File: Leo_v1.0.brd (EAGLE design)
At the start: 68.6 x 53.3 mm, 60 parts, among them CN1 POWER_JACK, CN2 47346-0001, CN3 DIGITAL10, CN4 DIGITAL8, CN5 ICSP, CN6 POWER8, CN7 ANALOG6, IC1 AMS1117-5.0, IC2 AMS1117-3.3, IC3 MCP6002T-I/SN, Q1 12MHz, Q2 16MHz, T1 AO3401A, T2 2N7002, U1 CH340G

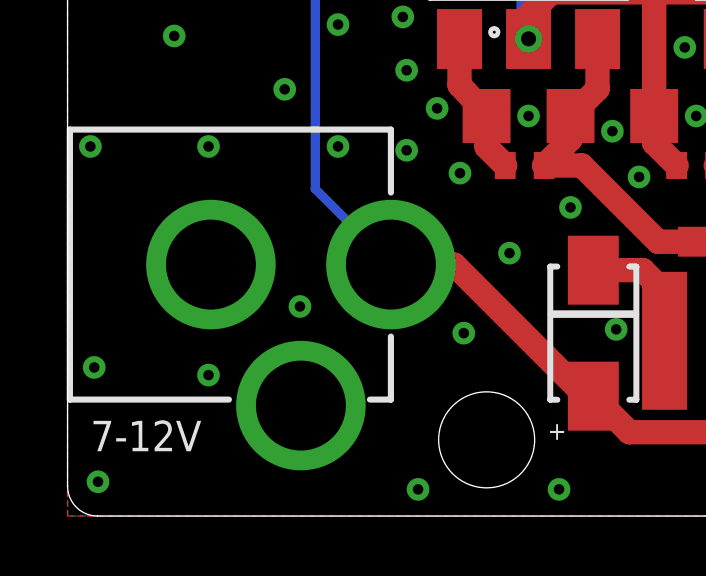
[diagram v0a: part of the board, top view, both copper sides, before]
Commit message: Add extra traces around power jack.
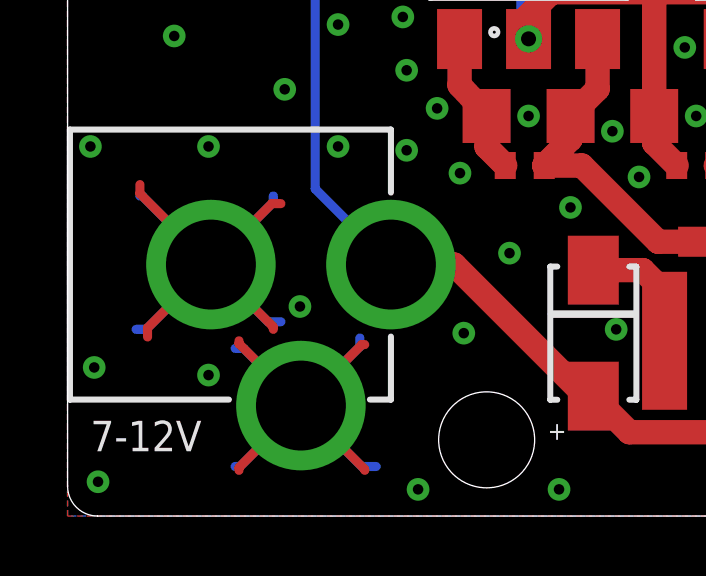
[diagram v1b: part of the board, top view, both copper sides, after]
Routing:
- net GND: track 52.0 -> 102.5 mm

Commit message: Add some routing for Leo.
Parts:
- removed C10: 12pF, rcl:C0402
- removed C18, C8: 100nF, rcl:C0402
- removed Q1: 12MHz, crystal-geyer_V1_0:3.2X2.5_KX-7
- removed R11: 1K, rcl:R0402
- removed SJ1: USB_RESET, _my_jumpers:SJ
- added L3: GZ2012D601TF, Wurth_Automotive_WE-CBA:WE-CBA_0805(W=4)
- added U2: ATMEGA32U4-AU, SparkFun-IC-Microcontroller:TQFP44
- C7: value 100nF -> 1uF; device rcl:C0402 -> rcl:C0603
- C9: value 12pF -> 100nF
- R3: value 1M -> 10K
- U1: value CH340G -> ATMEGA32U4-MU; device SparkFun-IC-Comms:SO016 -> SparkFun-IC-Microcontroller:QFN-44
- moved C7 43.2 mm to (59.7, 30.7)
- moved C9 36.5 mm to (54.9, 23.4), turned to 180 degrees
- moved U1 35.0 mm to (51.1, 30.7), turned to 180 degrees
- moved R3 27.1 mm to (43.8, 26.0), turned to 90 degrees
- moved R12 25.6 mm to (55.1, 38.2), turned to 0 degrees
- moved C14 13.9 mm to (59.8, 27.3)
- moved C12 7.12 mm to (51.9, 40.9)
- moved C13 7.12 mm to (49.1, 40.9)
- moved Q2 7.12 mm to (50.7, 43.1)
- moved R6 7.12 mm to (51.1, 39.5)
- moved C17 6.08 mm to (55.1, 41.0), turned to 180 degrees
- moved C15 6.03 mm to (54.0, 39.4), turned to 180 degrees
- moved C19 5.72 mm to (53.6, 22.0)
- moved C16 1.15 mm to (46.7, 22.9)
- moved R4 0.64 mm to (9.91, 31.1)
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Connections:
- removed net A4_SDA: CN3.2, CN7.2
- removed net A5_SCL: CN3.1, CN7.1
- removed net D2: CN4.6
- removed net D3_PWM: CN4.5
- removed net N$5: C18.2, SJ1.1
- removed net N$6: C7.2, U1.4
- removed net USB_DTR: C18.1, R11.2, U1.13
- removed net USB_OSC_IN: C9.2, Q1.3, R3.2, U1.7
- removed net USB_OSC_OUT: C10.2, Q1.1, R3.1, U1.8
- new net A4: CN7.2, U1.40, U2.40
- new net A5: CN7.1, U1.41, U2.41
- new net AVCC: C9.1, L3.1, U1.24, U1.44, U2.24, U2.44
- new net D2_SDA: CN3.2, CN4.6, U1.19, U2.19
- new net D3_SCL: CN3.1, CN4.5, U1.18, U2.18
- new net HWB: R3.2, U1.33, U2.33
- new net RX_LED: R8.1, U1.8, U2.8
- new net SPI_MISO: CN5.1, U1.11, U2.11
- new net SPI_MOSI: CN5.4, U1.10, U2.10
- new net SPI_SCK: CN5.3, U1.9, U2.9
- new net TX_LED: R9.1, U1.22, U2.22
- new net UCAP: C7.1, U1.6, U2.6
- net 5V: now also L3.2, U1.14, U1.2, U1.34, U2.14, U2.2, U2.34; no longer C8.1, U1.16
- net A0: now also U1.36, U2.36
- net A1: now also U1.37, U2.37
- net A2: now also U1.38, U2.38
- net A3: now also U1.39, U2.39
- net AREF: now also U1.42, U2.42
- net D0_RX: now also U1.20, U2.20; no longer R8.1, U1.2
- net D10_SS: now also U1.30, U2.30
- net D11_MOSI: now also U1.12, U2.12; no longer CN5.4
- net D12_MISO: now also U1.26, U2.26; no longer CN5.1
- net D13_SCK: now also U1.32, U2.32; no longer CN5.3
- net D1_TX: now also U1.21, U2.21; no longer R9.1, U1.3
- net D4: now also U1.25, U2.25
- net D5_PWM: now also U1.31, U2.31
- net D6_PWM: now also U1.27, U2.27
- net D7: now also U1.1, U2.1
- net D8: now also U1.28, U2.28
- net D9_PWM: now also U1.29, U2.29
- net GND: now also C7.2, C9.2, R3.1, U1.15, U1.23, U1.35, U1.43, U1.5, U2.15, U2.23, U2.35, U2.43, U2.5; no longer C10.1, C7.1, C8.2, C9.1, R11.1, U1.1
- net MCU_OSC_IN: now also U1.16, U2.16
- net MCU_OSC_OUT: now also U1.17, U2.17
- net RESET: now also U1.13, U2.13; no longer SJ1.2
- net USB_D_M: now also U1.3, U2.3; no longer U1.6
- net USB_D_P: now also U1.4, U2.4; no longer U1.5
- net VUSB: now also U1.7, U2.7
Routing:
- net A5_SCL: track 92.3 -> 0.00 mm, vias 2 -> 0
- net A4_SDA: track 89.7 -> 0.00 mm, vias 2 -> 0
- net RX_LED: track 0.00 -> 81.7 mm, vias 0 -> 4
- net VUSB: track 18.9 -> 83.8 mm, vias 2 -> 4
- net D1_TX: track 91.9 -> 31.4 mm, vias 4 -> 2
- net TX_LED: track 0.00 -> 57.8 mm, vias 0 -> 2
- net D2_SDA: track 0.00 -> 56.8 mm, vias 0 -> 3
- net D0_RX: track 87.7 -> 32.8 mm, vias 4 -> 2
- net D3_SCL: track 0.00 -> 54.5 mm, vias 0 -> 2
- net USB_D_P: track 8.97 -> 56.2 mm, vias 0 -> 2
- net USB_D_M: track 8.91 -> 56.1 mm, vias 0 -> 2
- net D12_MISO: track 69.0 -> 30.9 mm, vias 3 -> 1
- net A5: track 0.00 -> 29.5 mm, vias 0 -> 1
- net AVCC: track 0.00 -> 28.8 mm, vias 0 -> 2
- net A4: track 0.00 -> 28.7 mm, vias 0 -> 1
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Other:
- board text added: "LEO"
- board text removed: "UNO"

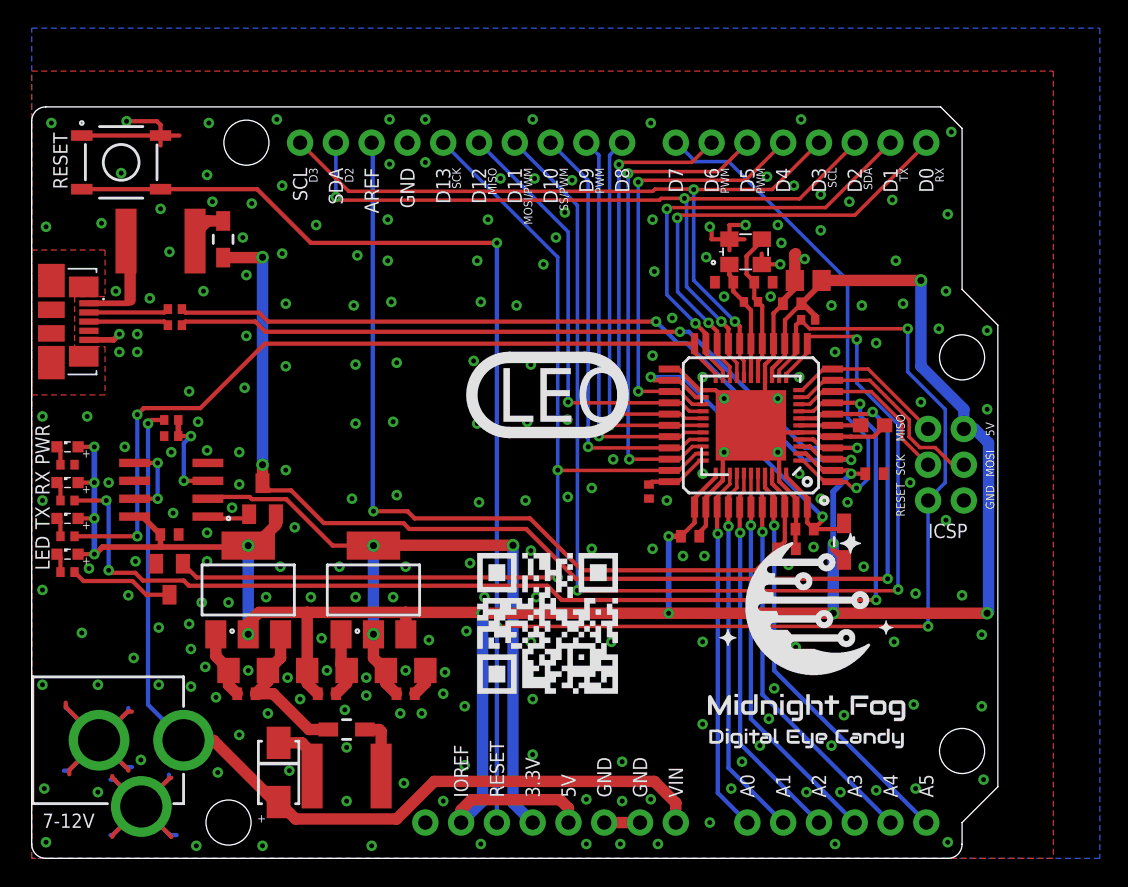
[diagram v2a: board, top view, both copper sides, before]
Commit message: Moved some traces around
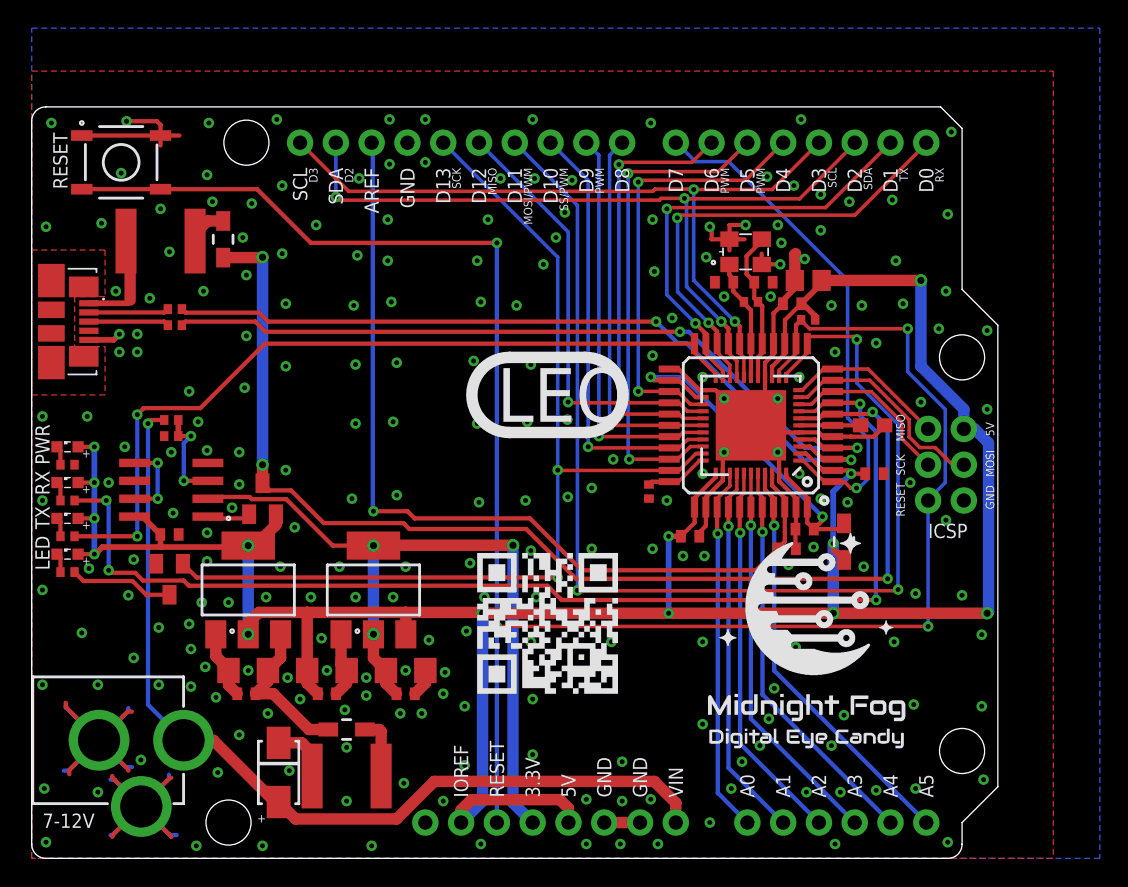
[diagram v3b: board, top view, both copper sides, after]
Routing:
- net GND: vias 231 -> 232

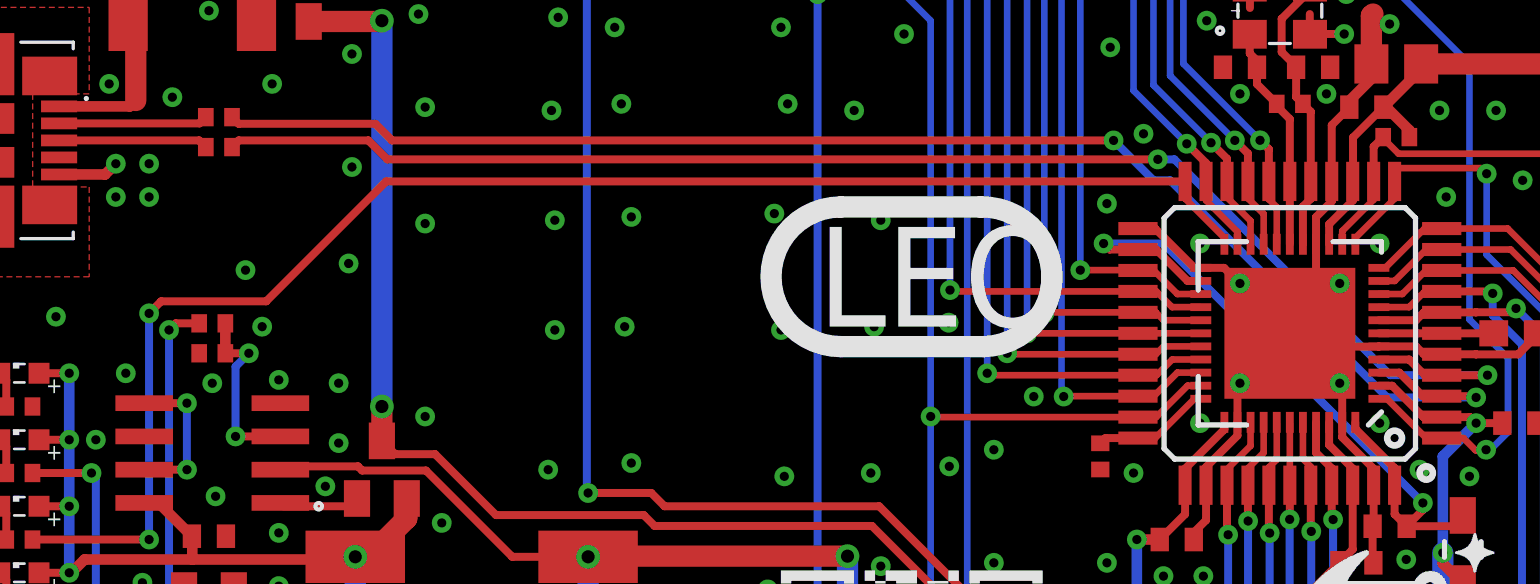
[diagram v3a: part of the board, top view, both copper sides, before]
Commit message: Moved TX_LED line away from USB lines to prevent interference.
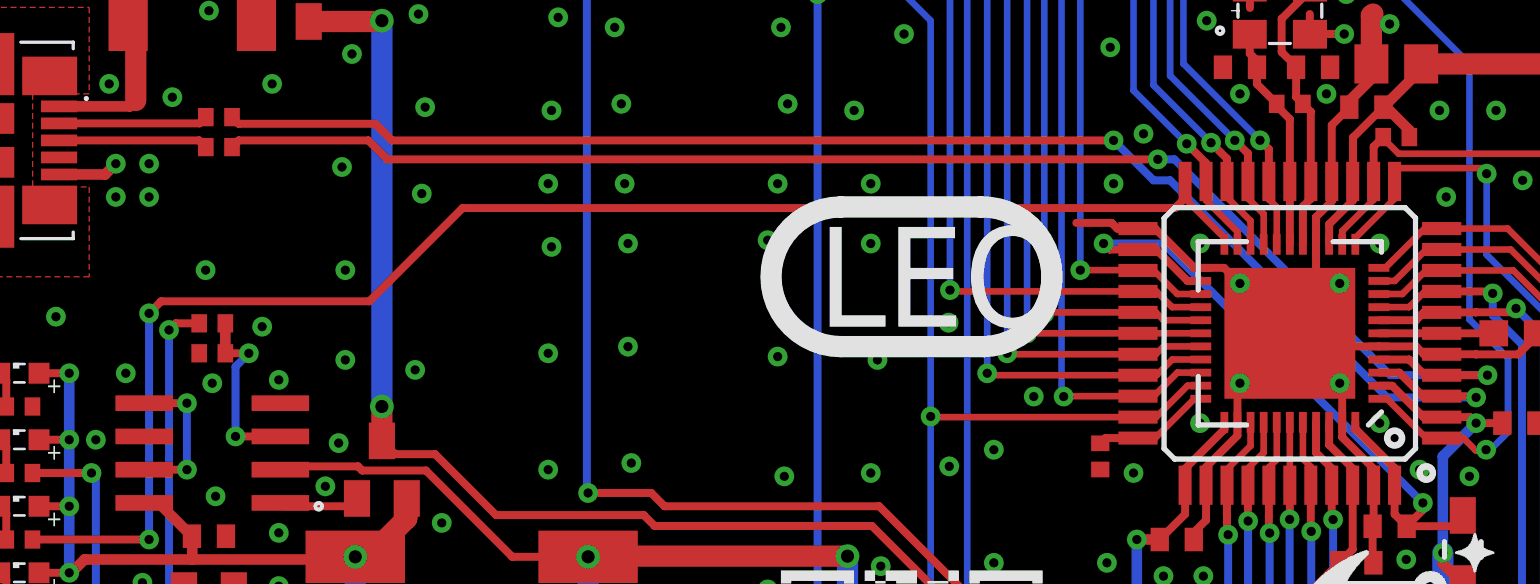
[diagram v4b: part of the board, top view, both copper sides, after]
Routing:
- net GND: track 124.3 -> 127.0 mm, vias 232 -> 236
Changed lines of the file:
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@@
 <via x="50.673" y="44.958" extent="1-16" drill="0.35"/>
 <via x="49.149" y="39.878" extent="1-16" drill="0.35"/>
-<via x="18.034" y="34.925" extent="1-16" drill="0.35"/>
+<via x="17.907" y="36.068" extent="1-16" drill="0.35"/>
 <via x="22.733" y="25.527" extent="1-16" drill="0.35"/>
 <via x="18.669" y="23.495" extent="1-16" drill="0.35"/>
@@
 <via x="9.144" y="46.101" extent="1-16" drill="0.35"/>
 <via x="14.732" y="26.543" extent="1-16" drill="0.35"/>
-<via x="22.987" y="30.861" extent="1-16" drill="0.35"/>
-<via x="14.732" y="28.829" extent="1-16" drill="0.35"/>
+<via x="22.86" y="34.036" extent="1-16" drill="0.35"/>
+<via x="14.986" y="29.718" extent="1-16" drill="0.35"/>
 <via x="12.446" y="23.114" extent="1-16" drill="0.35"/>
 <via x="9.906" y="28.829" extent="1-16" drill="0.35"/>
@@
 <via x="67.564" y="5.588" extent="1-16" drill="0.35"/>
 <via x="65.024" y="1.143" extent="1-16" drill="0.35"/>
-<via x="15.24" y="37.084" extent="1-16" drill="0.35"/>
+<via x="14.859" y="37.084" extent="1-16" drill="0.35"/>
 <via x="14.986" y="44.069" extent="1-16" drill="0.35"/>
 <via x="15.621" y="46.482" extent="1-16" drill="0.35"/>
@@
 <wire x1="5.812" y1="36.8" x2="6.223" y2="37.211" width="0.4064" layer="1"/>
 <via x="35.052" y="25.4" extent="1-16" drill="0.35"/>
-<via x="31.623" y="30.861" extent="1-16" drill="0.35"/>
-<via x="35.179" y="30.988" extent="1-16" drill="0.35"/>
+<via x="31.115" y="34.29" extent="1-16" drill="0.35"/>
+<via x="35.052" y="34.163" extent="1-16" drill="0.35"/>
 <via x="41.91" y="4.064" extent="1-16" drill="0.35"/>
 <via x="44.45" y="1.016" extent="1-16" drill="0.35"/>
@@
 <via x="15.24" y="41.402" extent="1-16" drill="0.35"/>
 <via x="17.78" y="42.926" extent="1-16" drill="0.35"/>
-<via x="18.034" y="27.559" extent="1-16" drill="0.35"/>
-<via x="25.654" y="30.988" extent="1-16" drill="0.35"/>
+<via x="17.653" y="29.337" extent="1-16" drill="0.35"/>
+<via x="25.781" y="34.163" extent="1-16" drill="0.35"/>
 <via x="25.908" y="25.781" extent="1-16" drill="0.35"/>
-<via x="11.176" y="33.147" extent="1-16" drill="0.35"/>
-<via x="22.987" y="35.052" extent="1-16" drill="0.35"/>
+<via x="9.652" y="33.147" extent="1-16" drill="0.35"/>
+<via x="22.733" y="36.449" extent="1-16" drill="0.35"/>
 <via x="32.131" y="18.542" extent="1-16" drill="0.35"/>
 <via x="31.115" y="20.955" extent="1-16" drill="0.35"/>
@@
 <wire x1="52.054" y1="34.134" x2="52.054" y2="32.6658" width="0.3048" layer="1"/>
 <wire x1="52.054" y1="32.6658" x2="52.07" y2="32.6498" width="0.3048" layer="1"/>
-<wire x1="54.454" y1="30.234" x2="54.446" y2="30.226" width="0.3048" layer="1"/>
-<wire x1="54.446" y1="30.226" x2="52.9698" y2="30.226" width="0.3048" layer="1"/>
 <wire x1="53.054" y1="27.334" x2="53.054" y2="28.5962" width="0.3048" layer="1"/>
 <wire x1="53.054" y1="28.5962" x2="52.959" y2="28.6912" width="0.3048" layer="1"/>
@@
 <via x="44.069" y="45.339" extent="1-16" drill="0.35"/>
 <via x="44.196" y="41.656" extent="1-16" drill="0.35"/>
-<via x="44.069" y="35.687" extent="1-16" drill="0.35"/>
+<via x="44.323" y="36.449" extent="1-16" drill="0.35"/>
 <via x="56.007" y="25.527" extent="1-16" drill="0.35"/>
 <via x="57.912" y="25.273" extent="1-16" drill="0.35"/>
@@
 <via x="31.877" y="39.497" extent="1-16" drill="0.35"/>
 <via x="25.527" y="39.497" extent="1-16" drill="0.35"/>
-<via x="31.369" y="35.306" extent="1-16" drill="0.35"/>
-<via x="25.908" y="35.179" extent="1-16" drill="0.35"/>
+<via x="31.496" y="36.449" extent="1-16" drill="0.35"/>
+<via x="25.654" y="36.449" extent="1-16" drill="0.35"/>
 <via x="22.86" y="39.243" extent="1-16" drill="0.35"/>
 <via x="23.114" y="42.799" extent="1-16" drill="0.35"/>
@@
 <via x="17.78" y="47.752" extent="1-16" drill="0.35"/>
 <via x="18.034" y="39.37" extent="1-16" drill="0.35"/>
-<via x="15.113" y="33.401" extent="1-16" drill="0.35"/>
+<via x="14.986" y="33.147" extent="1-16" drill="0.35"/>
 <via x="11.811" y="30.988" extent="1-16" drill="0.35"/>
 <via x="6.604" y="29.21" extent="1-16" drill="0.35"/>
@@
 <via x="62.611" y="10.922" extent="1-16" drill="0.35"/>
 <via x="34.417" y="39.243" extent="1-16" drill="0.35"/>
-<via x="35.433" y="35.052" extent="1-16" drill="0.35"/>
+<via x="35.052" y="36.449" extent="1-16" drill="0.35"/>
 <via x="38.0238" y="31.1404" extent="1-16" drill="0.35"/>
 <via x="38.0492" y="25.654" extent="1-16" drill="0.35"/>
@@
 <wire x1="54.168" y1="42.865" x2="54.229" y2="42.926" width="0.8128" layer="1"/>
 <via x="23.241" y="48.26" extent="1-16" drill="0.35"/>
+<wire x1="45.254" y1="34.734" x2="44.4639125" y2="34.734" width="0.3048" layer="1"/>
+<wire x1="44.4639125" y1="34.734" x2="44.2475125" y2="34.9504" width="0.3048" layer="1"/>
+<wire x1="44.2475125" y1="34.9504" x2="42.9006" y2="34.9504" width="0.3048" layer="1"/>
+<wire x1="54.454" y1="30.234" x2="52.7238" y2="30.234" width="0.3048" layer="1"/>
+<wire x1="52.7238" y1="30.234" x2="52.7158" y2="30.226" width="0.3048" layer="1"/>
+<via x="22.733" y="29.972" extent="1-16" drill="0.35"/>
+<via x="25.781" y="30.226" extent="1-16" drill="0.35"/>
+<via x="31.496" y="29.845" extent="1-16" drill="0.35"/>
+<via x="35.306" y="29.718" extent="1-16" drill="0.35"/>
 </signal>
 <signal name="VIN" class="3">
@@
 <wire x1="48.554" y1="34.377" x2="47.054" y2="35.877" width="0.254" layer="1"/>
 <via x="7.493" y="31.496" extent="1-16" drill="0.35"/>
-<wire x1="47.054" y1="36.534" x2="16.5449125" y2="36.534" width="0.3048" layer="1"/>
+<wire x1="47.054" y1="36.534" x2="47.054" y2="35.899" width="0.3048" layer="1"/>
+<wire x1="47.054" y1="35.899" x2="46.673" y2="35.518" width="0.3048" layer="1"/>
+<wire x1="46.673" y1="35.518" x2="19.4659125" y2="35.518" width="0.3048" layer="1"/>
 <wire x1="7.953" y1="31.956" x2="7.493" y2="31.496" width="0.3048" layer="1"/>
-<wire x1="11.9669125" y1="31.956" x2="7.953" y2="31.956" width="0.3048" layer="1"/>
-<wire x1="16.5449125" y1="36.534" x2="11.9669125" y2="31.956" width="0.3048" layer="1"/>
+<wire x1="15.9039125" y1="31.956" x2="7.953" y2="31.956" width="0.3048" layer="1"/>
+<wire x1="19.4659125" y1="35.518" x2="15.9039125" y2="31.956" width="0.3048" layer="1"/>
 <wire x1="7.493" y1="31.496" x2="7.493" y2="22.86" width="0.3048" layer="16"/>
 <via x="7.493" y="22.86" extent="1-16" drill="0.35"/>
